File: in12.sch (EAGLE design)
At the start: 34 parts, among them U1 MICROCHIP_HV5622PG-GMICROCHIP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, U2 MICROCHIP_HV5622PG-GMICROCHIP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, U3 MICROCHIP_HV5622PG-GMICROCHIP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

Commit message: 5523 still need shuffle pins
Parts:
- removed U1, U2, U3: MICROCHIP_HV5622PG-GMICROCHIP_HV5622PG-G_0_0, Microchip - HV5622PG-G:MICROCHIP_HV5622PG-GMICROCHIP_HV5622PG-G_0_0
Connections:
- net L10: no longer U1.HVOUT32
- net L11: no longer U1.HVOUT27
- net L12: no longer U1.HVOUT23
- net L13: no longer U1.HVOUT24
- net L14: no longer U1.HVOUT25
- net L15: no longer U1.HVOUT26
- net L16: no longer U1.HVOUT28
- net L17: no longer U1.HVOUT30
- net L18: no longer U1.HVOUT31
- net L19: no longer U1.HVOUT29
- net L1D: no longer U1.HVOUT22
- net L20: no longer U1.HVOUT21
- net L21: no longer U1.HVOUT16
- net L22: no longer U1.HVOUT12
- net L23: no longer U1.HVOUT13
- net L24: no longer U1.HVOUT14
- net L25: no longer U1.HVOUT15
- net L26: no longer U1.HVOUT17
- net L27: no longer U1.HVOUT19
- net L28: no longer U1.HVOUT20
- net L29: no longer U1.HVOUT18
- net L2D: no longer U1.HVOUT1
- net L30: no longer U1.HVOUT11
- net L31: no longer U1.HVOUT6
- net L32: no longer U1.HVOUT2
- net L33: no longer U1.HVOUT3
- net L34: no longer U1.HVOUT4
- net L35: no longer U1.HVOUT5
- net L36: no longer U1.HVOUT7
- net L37: no longer U1.HVOUT9
- net L38: no longer U1.HVOUT10
- net L39: no longer U1.HVOUT8
- net L3D: now also U5.HV1; no longer U2.HVOUT32
- net L40: now also U5.HV2; no longer U2.HVOUT31
- net L41: now also U5.HV7; no longer U2.HVOUT26
- net L42: now also U5.HV14; no longer U2.HVOUT19
- net L43: now also U5.HV12; no longer U2.HVOUT21
- net L44: now also U5.HV9; no longer U2.HVOUT24
- net L45: now also U5.HV8; no longer U2.HVOUT25
- net L46: now also U5.HV6; no longer U2.HVOUT27
- net L47: now also U5.HV4; no longer U2.HVOUT29
- net L48: now also U5.HV3; no longer U2.HVOUT30
- net L49: now also U5.HV5; no longer U2.HVOUT28
- net L4D: now also U5.HV15; no longer U2.HVOUT18
- net L50: now also U5.HV17; no longer U2.HVOUT16
- net L51: now also U5.HV23; no longer U2.HVOUT10
- net L52: now also U5.HV27; no longer U2.HVOUT6
- net L53: now also U5.HV26; no longer U2.HVOUT7
- net L54: now also U5.HV25; no longer U2.HVOUT8
- net L55: now also U5.HV24; no longer U2.HVOUT9
- net L56: now also U5.HV22; no longer U2.HVOUT11
- net L57: now also U5.HV20; no longer U2.HVOUT13
- net L58: now also U5.HV18; no longer U2.HVOUT15
- net L59: now also U5.HV21; no longer U2.HVOUT12
- net L5D: now also U5.HV28; no longer U2.HVOUT5
- net L60: now also U5.HV29; no longer U2.HVOUT4
- net L61: now also U6.HV2; no longer U3.HVOUT31
- net L62: now also U6.HV9; no longer U3.HVOUT24
- net L63: now also U6.HV8; no longer U3.HVOUT25
- net L64: now also U6.HV4; no longer U3.HVOUT29
- net L65: now also U6.HV3; no longer U3.HVOUT30
- net L66: now also U6.HV1; no longer U3.HVOUT32
- net L67: now also U5.HV32; no longer U2.HVOUT1
- net L68: now also U5.HV31; no longer U2.HVOUT2
- net L69: now also U5.HV30; no longer U2.HVOUT3
- net L6D: now also U6.HV10; no longer U3.HVOUT23
- net L70: now also U6.HV11; no longer U3.HVOUT22
- net L71: now also U6.HV16; no longer U3.HVOUT17
- net L72: now also U6.HV20; no longer U3.HVOUT13
- net L73: now also U6.HV19; no longer U3.HVOUT14
- net L74: now also U6.HV18; no longer U3.HVOUT15
- net L75: now also U6.HV17; no longer U3.HVOUT16
- net L76: now also U6.HV15; no longer U3.HVOUT18
- net L77: now also U6.HV13; no longer U3.HVOUT20
- net L78: now also U6.HV12; no longer U3.HVOUT21
- net L79: now also U6.HV14; no longer U3.HVOUT19
- net L7D: now also U6.HV21; no longer U3.HVOUT12
- net L80: now also U6.HV22; no longer U3.HVOUT11
- net L81: now also U6.HV27; no longer U3.HVOUT6
- net L82: now also U6.HV31; no longer U3.HVOUT2
- net L83: now also U6.HV30; no longer U3.HVOUT3
- net L84: now also U6.HV29; no longer U3.HVOUT4
- net L85: now also U6.HV28; no longer U3.HVOUT5
- net L86: now also U6.HV26; no longer U3.HVOUT7
- net L87: now also U6.HV24; no longer U3.HVOUT9
- net L88: now also U6.HV23; no longer U3.HVOUT10
- net L89: now also U6.HV25; no longer U3.HVOUT8
- net L8D: now also U6.HV32; no longer U3.HVOUT1
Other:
- moved on the sheet: SV1, SV2, SV3, SV4, U4, U5, U6

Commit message: hv single layer routed
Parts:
- added U$1: DS3232, ds3232:DS3232
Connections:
- net L2D: now also U4.HV22; no longer U4.HV32
- net L30: now also U4.HV23; no longer U4.HV22
- net L31: now also U4.HV28; no longer U4.HV27
- net L32: now also U4.HV32; no longer U4.HV31
- net L33: now also U4.HV31; no longer U4.HV30
- net L34: now also U4.HV30; no longer U4.HV29
- net L35: now also U4.HV29; no longer U4.HV28
- net L36: now also U4.HV27; no longer U4.HV26
- net L37: now also U4.HV25; no longer U4.HV24
- net L38: now also U4.HV24; no longer U4.HV23
- net L39: now also U4.HV26; no longer U4.HV25
- net L41: now also U5.HV8; no longer U5.HV7
- net L42: now also U5.HV11; no longer U5.HV14
- net L43: now also U5.HV10; no longer U5.HV12
- net L45: now also U5.HV7; no longer U5.HV8
- net L4D: now also U5.HV12; no longer U5.HV15
- net L50: now also U5.HV13; no longer U5.HV17
- net L51: now also U5.HV18; no longer U5.HV23
- net L52: now also U5.HV22; no longer U5.HV27
- net L53: now also U5.HV21; no longer U5.HV26
- net L54: now also U5.HV20; no longer U5.HV25
- net L55: now also U5.HV19; no longer U5.HV24
- net L56: now also U5.HV17; no longer U5.HV22
- net L57: now also U5.HV15; no longer U5.HV20
- net L58: now also U5.HV14; no longer U5.HV18
- net L59: now also U5.HV16; no longer U5.HV21
- net L5D: now also U5.HV23; no longer U5.HV28
- net L60: now also U5.HV24; no longer U5.HV29
- net L61: now also U6.HV5; no longer U6.HV2
- net L64: now also U6.HV7; no longer U6.HV4
- net L65: now also U6.HV6; no longer U6.HV3
- net L66: now also U6.HV4; no longer U6.HV1
- net L67: now also U6.HV3; no longer U5.HV32
- net L68: now also U6.HV2; no longer U5.HV31
- net L69: now also U6.HV1; no longer U5.HV30
- net L71: now also U6.HV15; no longer U6.HV16
- net L76: now also U6.HV16; no longer U6.HV15
- net L77: now also U6.HV14; no longer U6.HV13
- net L79: now also U6.HV13; no longer U6.HV14

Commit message: compact
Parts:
- added IC1: LM1117MPX-3.3_NOPB, SamacSys_Parts:LM1117MPX-3.3_NOPB
- added U$2: HV_PSU, SamacSys_Parts:HV_PSU
- added U1: ESP32-WROOM-32D, SamacSys_Parts:ESP32-WROOM-32D
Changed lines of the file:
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@@
 <part name="U6" library="nixiemisc" deviceset="HV5523" device=""/>
 <part name="U$1" library="ds3232" deviceset="DS3232" device=""/>
+<part name="U$2" library="SamacSys_Parts" deviceset="HV_PSU" device=""/>
+<part name="U1" library="SamacSys_Parts" deviceset="ESP32-WROOM-32D" device="" package3d_urn="urn:adsk.eagle:package:22977922/1"/>
+<part name="IC1" library="SamacSys_Parts" deviceset="LM1117MPX-3.3_NOPB" device="" package3d_urn="urn:adsk.eagle:package:22978087/1"/>
 </parts>
 <sheets>
@@
 </instance>
 <instance part="U$1" gate="G$1" x="276.86" y="147.32" smashed="yes"/>
+<instance part="U$2" gate="G$1" x="284.48" y="116.84" smashed="yes"/>
+<instance part="U1" gate="G$1" x="287.02" y="60.96" smashed="yes">
+<attribute name="NAME" x="271.9841" y="92.5545" size="1.778" layer="95"/>
+<attribute name="VALUE" x="271.7333" y="25.2919" size="1.778" layer="96"/>
+</instance>
+<instance part="IC1" gate="G$1" x="271.78" y="10.16" smashed="yes">
+<attribute name="NAME" x="300.99" y="17.78" size="1.778" layer="95" align="center-left"/>
+<attribute name="VALUE" x="300.99" y="15.24" size="1.778" layer="96" align="center-left"/>
+</instance>
 </instances>
 <busses>

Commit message: added m.2 connector
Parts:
- added J1: 1-2199230-6, 1-2199230-6:1-2199230-6
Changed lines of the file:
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@@
 <part name="U1" library="SamacSys_Parts" deviceset="ESP32-WROOM-32D" device="" package3d_urn="urn:adsk.eagle:package:22977922/1"/>
 <part name="IC1" library="SamacSys_Parts" deviceset="LM1117MPX-3.3_NOPB" device="" package3d_urn="urn:adsk.eagle:package:22978087/1"/>
+<part name="J1" library="1-2199230-6" deviceset="1-2199230-6" device=""/>
 </parts>
 <sheets>
@@
 <attribute name="VALUE" x="300.99" y="15.24" size="1.778" layer="96" align="center-left"/>
 </instance>
+<instance part="J1" gate="G$1" x="355.6" y="142.24" smashed="yes">
+<attribute name="NAME" x="347.93463125" y="194.0886" size="2.1974" layer="95"/>
+<attribute name="VALUE" x="347.94233125" y="88.6558" size="2.1952" layer="96"/>
+</instance>
 </instances>

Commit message: control board, adapter ffc wire
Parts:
- removed IC1: LM1117MPX-3.3_NOPB, SamacSys_Parts:LM1117MPX-3.3_NOPB
- removed SV1, SV2, SV3, SV4: (no value), con-lstb:MA05-1
- removed U$1: DS3232, ds3232:DS3232
- removed U$2: HV_PSU, SamacSys_Parts:HV_PSU
- removed U1: ESP32-WROOM-32D, SamacSys_Parts:ESP32-WROOM-32D
- J1: value 1-2199230-6 -> 1-2328702-0; device 1-2199230-6:1-2199230-6 -> 1-2328702-0:1-2328702-0
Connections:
- new net 3V3: J1.6, U4.VDD, U5.VDD, U6.VDD
- new net BL: J1.9, U4.!BL, U5.!BL, U6.!BL
- new net CLK: J1.4, U4.CLK, U5.CLK, U6.CLK
- new net GND: J1.5, U4.EXP, U4.VSS, U5.EXP, U5.VSS, U6.EXP, U6.VSS
- new net IN: J1.8, U4.DATAIN
- new net LE: J1.7, U4.!LE, U5.!LE, U6.!LE
- new net N$17: U4.DATAOUT, U5.DATAIN
- new net N$18: U5.DATAOUT, U6.DATAIN
- new net OUT: J1.10, U6.DATAOUT
- new net POL: J1.3, U4.!POL, U5.!POL, U6.!POL
- net HV: now also J1.1

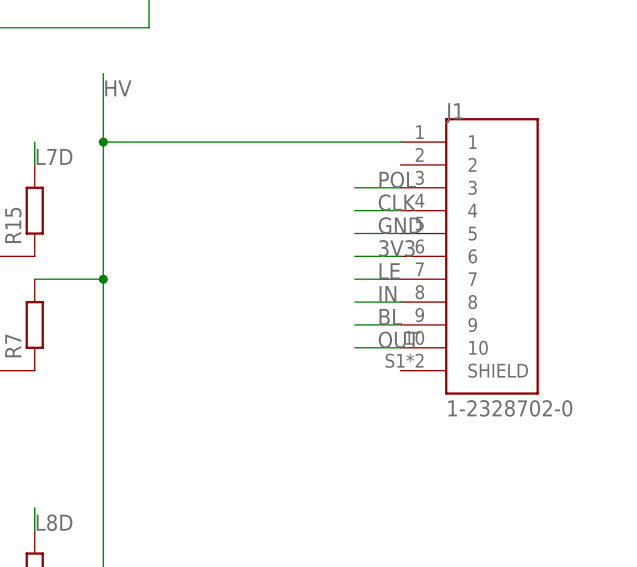
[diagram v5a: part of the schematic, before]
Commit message: routing connector
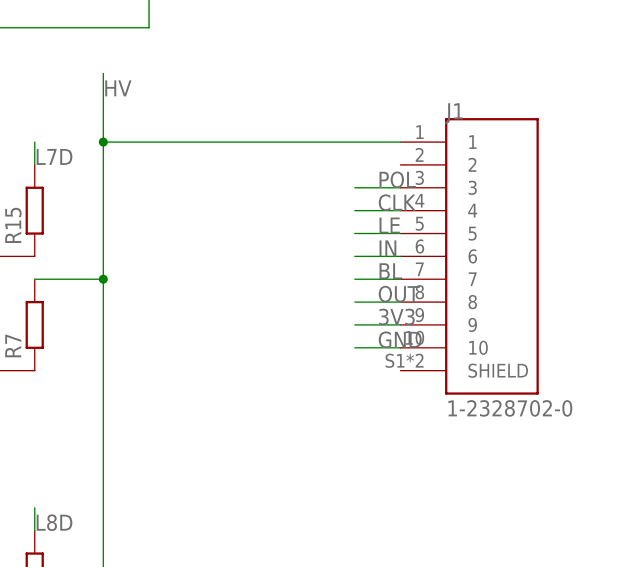
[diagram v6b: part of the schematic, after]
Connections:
- net 3V3: now also J1.9; no longer J1.6
- net BL: now also J1.7; no longer J1.9
- net GND: now also J1.10; no longer J1.5
- net IN: now also J1.6; no longer J1.8
- net LE: now also J1.5; no longer J1.7
- net OUT: now also J1.8; no longer J1.10
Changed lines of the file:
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@@
 </segment>
 <segment>
-<wire x1="256.54" y1="93.98" x2="261.62" y2="93.98" width="0.1524" layer="91"/>
-<label x="259.08" y="93.98" size="1.778" layer="95"/>
-<pinref part="J1" gate="G$1" pin="7"/>
+<wire x1="256.54" y1="99.06" x2="261.62" y2="99.06" width="0.1524" layer="91"/>
+<label x="259.08" y="99.06" size="1.778" layer="95"/>
+<pinref part="J1" gate="G$1" pin="5"/>
 </segment>
 </net>
@@
 </segment>
 <segment>
-<wire x1="256.54" y1="88.9" x2="261.62" y2="88.9" width="0.1524" layer="91"/>
-<label x="259.08" y="88.9" size="1.778" layer="95"/>
-<pinref part="J1" gate="G$1" pin="9"/>
+<wire x1="256.54" y1="93.98" x2="261.62" y2="93.98" width="0.1524" layer="91"/>
+<label x="259.08" y="93.98" size="1.778" layer="95"/>
+<pinref part="J1" gate="G$1" pin="7"/>
 </segment>
 </net>
@@
 </segment>
 <segment>
-<wire x1="256.54" y1="91.44" x2="261.62" y2="91.44" width="0.1524" layer="91"/>
-<label x="259.08" y="91.44" size="1.778" layer="95"/>
-<pinref part="J1" gate="G$1" pin="8"/>
+<wire x1="256.54" y1="96.52" x2="261.62" y2="96.52" width="0.1524" layer="91"/>
+<label x="259.08" y="96.52" size="1.778" layer="95"/>
+<pinref part="J1" gate="G$1" pin="6"/>
 </segment>
 </net>
@@
 </segment>
 <segment>
-<wire x1="256.54" y1="86.36" x2="261.62" y2="86.36" width="0.1524" layer="91"/>
-<label x="259.08" y="86.36" size="1.778" layer="95"/>
-<pinref part="J1" gate="G$1" pin="10"/>
+<wire x1="256.54" y1="91.44" x2="261.62" y2="91.44" width="0.1524" layer="91"/>
+<label x="259.08" y="91.44" size="1.778" layer="95"/>
+<pinref part="J1" gate="G$1" pin="8"/>
 </segment>
 </net>
@@
 </segment>
 <segment>
-<wire x1="256.54" y1="99.06" x2="261.62" y2="99.06" width="0.1524" layer="91"/>
-<label x="259.08" y="99.06" size="1.778" layer="95"/>
-<pinref part="J1" gate="G$1" pin="5"/>
+<wire x1="256.54" y1="86.36" x2="261.62" y2="86.36" width="0.1524" layer="91"/>
+<label x="259.08" y="86.36" size="1.778" layer="95"/>
+<pinref part="J1" gate="G$1" pin="10"/>
 </segment>
 </net>
@@
 </segment>
 <segment>
-<wire x1="256.54" y1="96.52" x2="261.62" y2="96.52" width="0.1524" layer="91"/>
-<label x="259.08" y="96.52" size="1.778" layer="95"/>
-<pinref part="J1" gate="G$1" pin="6"/>
+<wire x1="256.54" y1="88.9" x2="261.62" y2="88.9" width="0.1524" layer="91"/>
+<label x="259.08" y="88.9" size="1.778" layer="95"/>
+<pinref part="J1" gate="G$1" pin="9"/>
 </segment>
 </net>

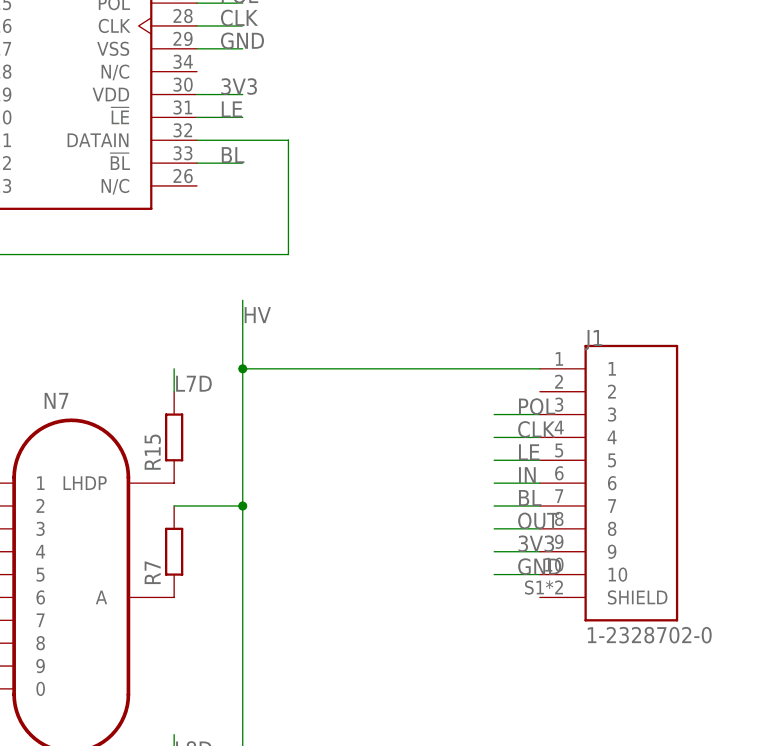
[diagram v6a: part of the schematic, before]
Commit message: lamp board finished, working on control
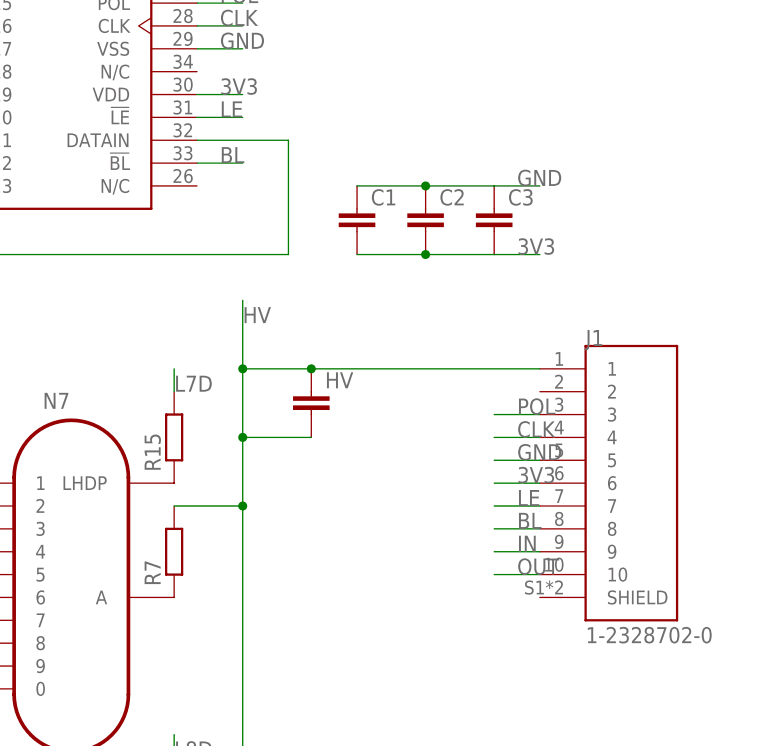
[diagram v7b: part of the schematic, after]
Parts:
- added C1, C2, C3: (no value), rcl:C-EUC0805
- added HV: (no value), rcl:C-EUC1206
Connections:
- net 3V3: now also C1.2, C2.2, C3.2, J1.6; no longer J1.9
- net BL: now also J1.8; no longer J1.7
- net GND: now also C1.1, C2.1, C3.1, J1.5; no longer J1.10
- net HV: now also HV.1, HV.2
- net IN: now also J1.9; no longer J1.6
- net LE: now also J1.7; no longer J1.5
- net OUT: now also J1.10; no longer J1.8
